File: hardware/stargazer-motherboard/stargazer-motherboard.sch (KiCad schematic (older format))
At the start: 13 parts, among them J1_n swd-header, J2_n swd-flywire, J3_n feather-leftovers, U1_n ADAFRUIT_FEATHER, U2_n SN74LVC125AD

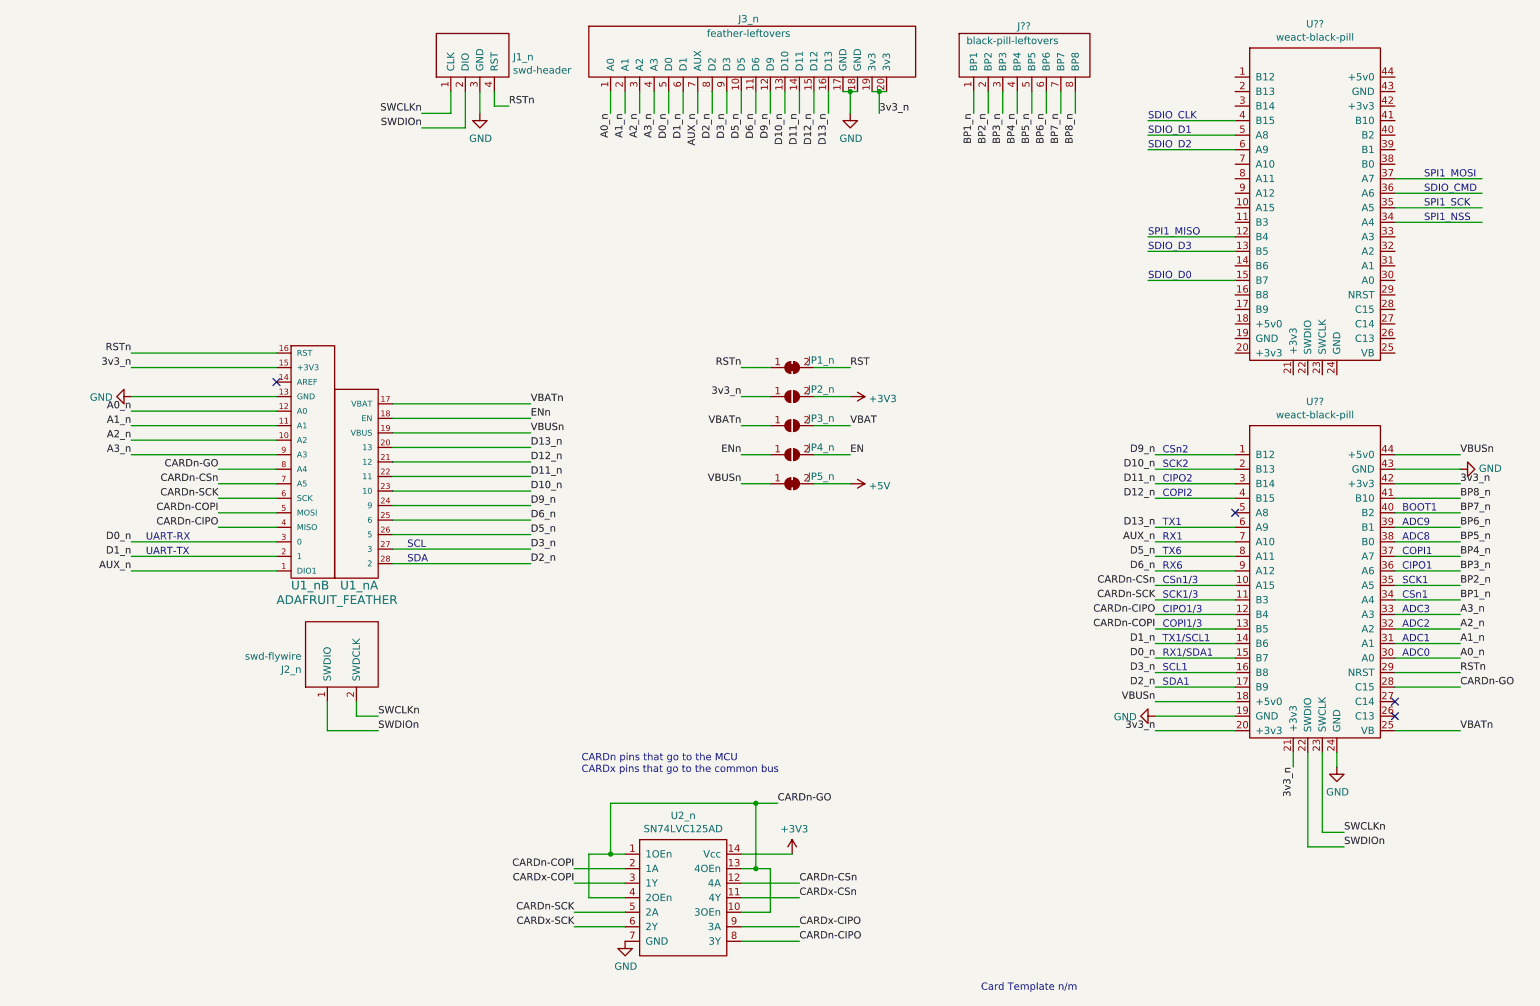
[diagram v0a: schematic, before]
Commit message: Some basic routing
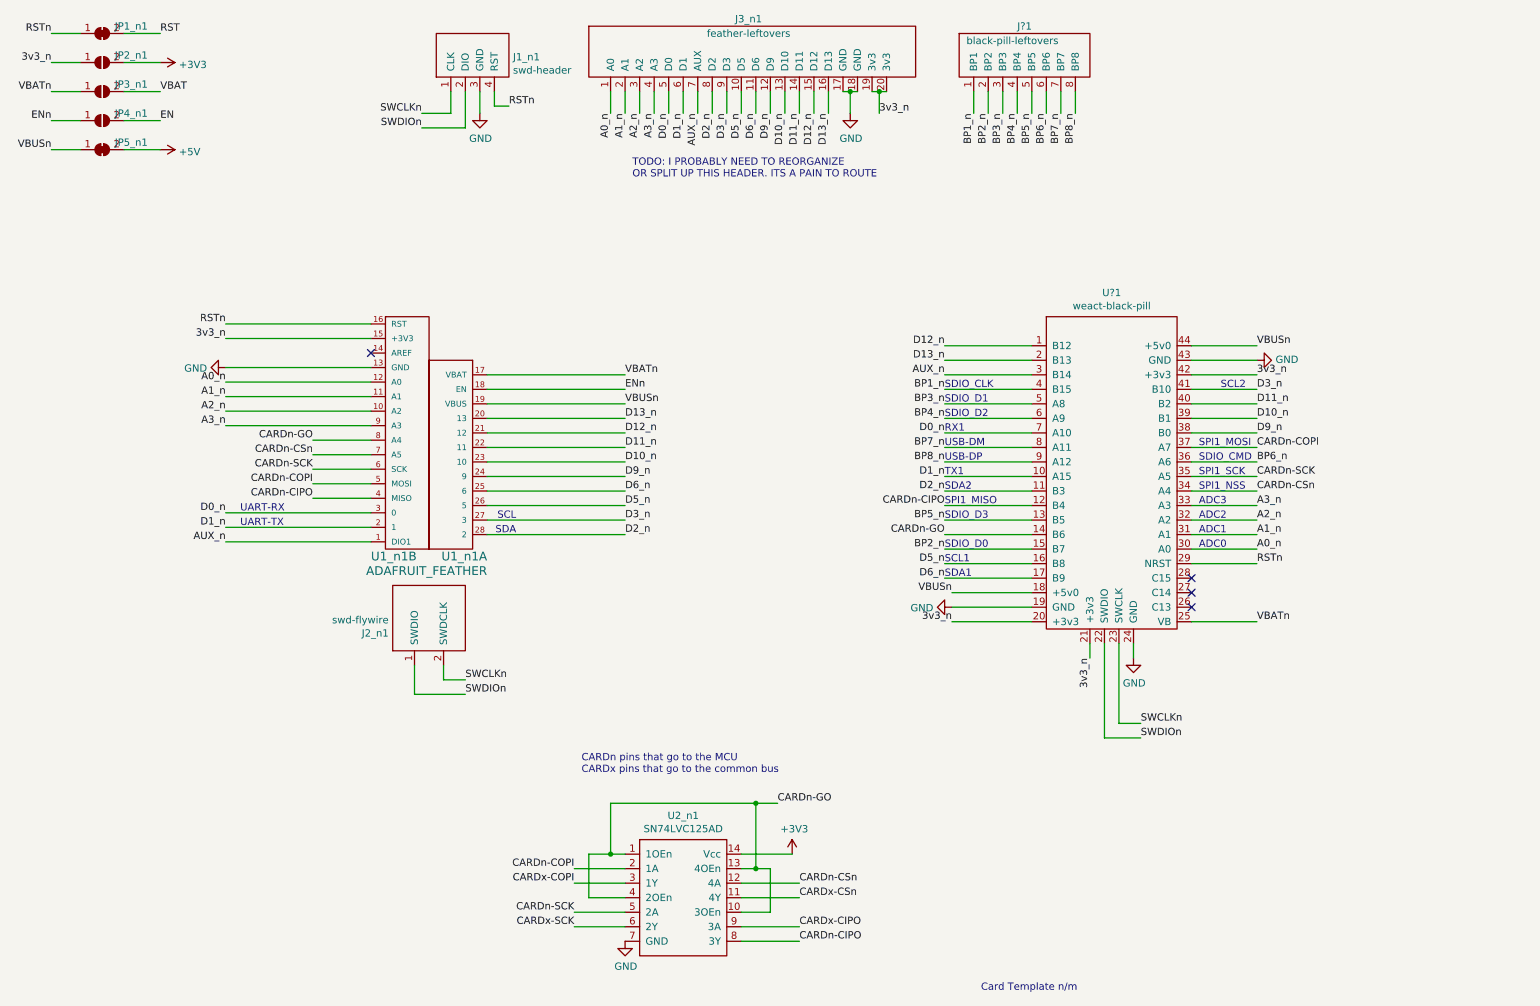
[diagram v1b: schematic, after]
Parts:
- removed U??: weact-black-pill, symbol stargazer:weact-black-pill
- J1_n1: renamed from J1_n; footprint (none) -> Connector_PinHeader_2.54mm:PinHeader_2x02_P2.54mm_Vertical
- J2_n1: renamed from J2_n; footprint (none) -> Connector_PinHeader_2.54mm:PinHeader_1x02_P2.54mm_Vertical
- J3_n1: renamed from J3_n; footprint (none) -> Connector_PinHeader_2.54mm:PinHeader_2x10_P2.54mm_Vertical
- J?1: renamed from J??; footprint (none) -> Connector_PinHeader_2.54mm:PinHeader_2x04_P2.54mm_Vertical
- JP1_n1: renamed from JP1_n; footprint (none) -> Jumper:SolderJumper-2_P1.3mm_Bridged_RoundedPad1.0x1.5mm
- JP2_n1: renamed from JP2_n; footprint (none) -> Jumper:SolderJumper-2_P1.3mm_Open_RoundedPad1.0x1.5mm
- JP3_n1: renamed from JP3_n; footprint (none) -> Jumper:SolderJumper-2_P1.3mm_Open_RoundedPad1.0x1.5mm
- JP4_n1: renamed from JP4_n; footprint (none) -> Jumper:SolderJumper-2_P1.3mm_Open_RoundedPad1.0x1.5mm
- JP5_n1: renamed from JP5_n; footprint (none) -> Jumper:SolderJumper-2_P1.3mm_Bridged_RoundedPad1.0x1.5mm
- U1_n1: renamed from U1_n; footprint (none) -> Modules:ADAFRUIT_FEATHER
- U2_n1: renamed from U2_n; footprint (none) -> Package_SO:SOIC-14_3.9x8.7mm_P1.27mm
- U?1: renamed from U??; footprint (none) -> stargazer-motherboard:weact-blackpill
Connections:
- wire segments 152 -> 142
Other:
- note added: "SCL1\n"
- note added: "SCL2"
- note added: "SDA2"
- note added: "TODO: I PROBABLY NEED TO REORGANIZE\nOR SPLIT UP THIS HEADER. ITS A PAIN TO ROUTE"
- note added: "USB-DM"
- note added: "USB-DP"
- note removed: "ADC8"
- note removed: "ADC9"
- note removed: "BOOT1"
- note removed: "CIPO1"
- note removed: "CIPO1/3"
- note removed: "CIPO2"
- note removed: "COPI1"
- note removed: "COPI1/3"
- note removed: "COPI2"
- note removed: "CSn1"
- note removed: "CSn1/3"
- note removed: "CSn2"
- note removed: "RX1/SDA1"
- note removed: "RX6"
- note removed: "SCK1"
- note removed: "SCK1/3"
- note removed: "SCK2"
- note removed: "SCL1"
- note removed: "TX1/SCL1"
- note removed: "TX6"
- moved on the sheet: J2_n1, JP1_n1, JP2_n1, JP3_n1, JP4_n1, JP5_n1, U?1

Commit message: Now with thicc spaghetti
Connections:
- net D11_n: now also U?1.38 (B0); no longer U?1.40 (B2)
- net D9_n: now also U?1.40 (B2); no longer U?1.38 (B0)
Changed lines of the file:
@@
 Wire Wire Line
 	8850 3250 9300 3250
-Text Label 9300 3650 0    50   ~ 0
+Text Label 9300 3450 0    50   ~ 0
 D9_n
 Text Label 9300 3550 0    50   ~ 0
 D10_n
-Text Label 9300 3450 0    50   ~ 0
+Text Label 9300 3650 0    50   ~ 0
 D11_n
 Text Label 7150 3050 2    50   ~ 0
@@
 Wire Wire Line
 	7150 3250 7750 3250
-Wire Wire Line
-	8850 3650 9300 3650
-Wire Wire Line
-	9300 3550 8850 3550
-Wire Wire Line
-	8850 3450 9300 3450
 Text Label 9300 4550 0    50   ~ 0
 RSTn
@@
 Text Notes 5000 1900 0    50   ~ 0
 TODO: I PROBABLY NEED TO REORGANIZE\nOR SPLIT UP THIS HEADER. ITS A PAIN TO ROUTE
+Wire Wire Line
+	8850 3650 9300 3650
+Wire Wire Line
+	9300 3550 8850 3550
+Wire Wire Line
+	8850 3450 9300 3450
 $EndSCHEMATC
